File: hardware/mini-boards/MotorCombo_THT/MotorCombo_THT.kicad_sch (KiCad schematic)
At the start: 26 parts, among them J7 Conn_01x02

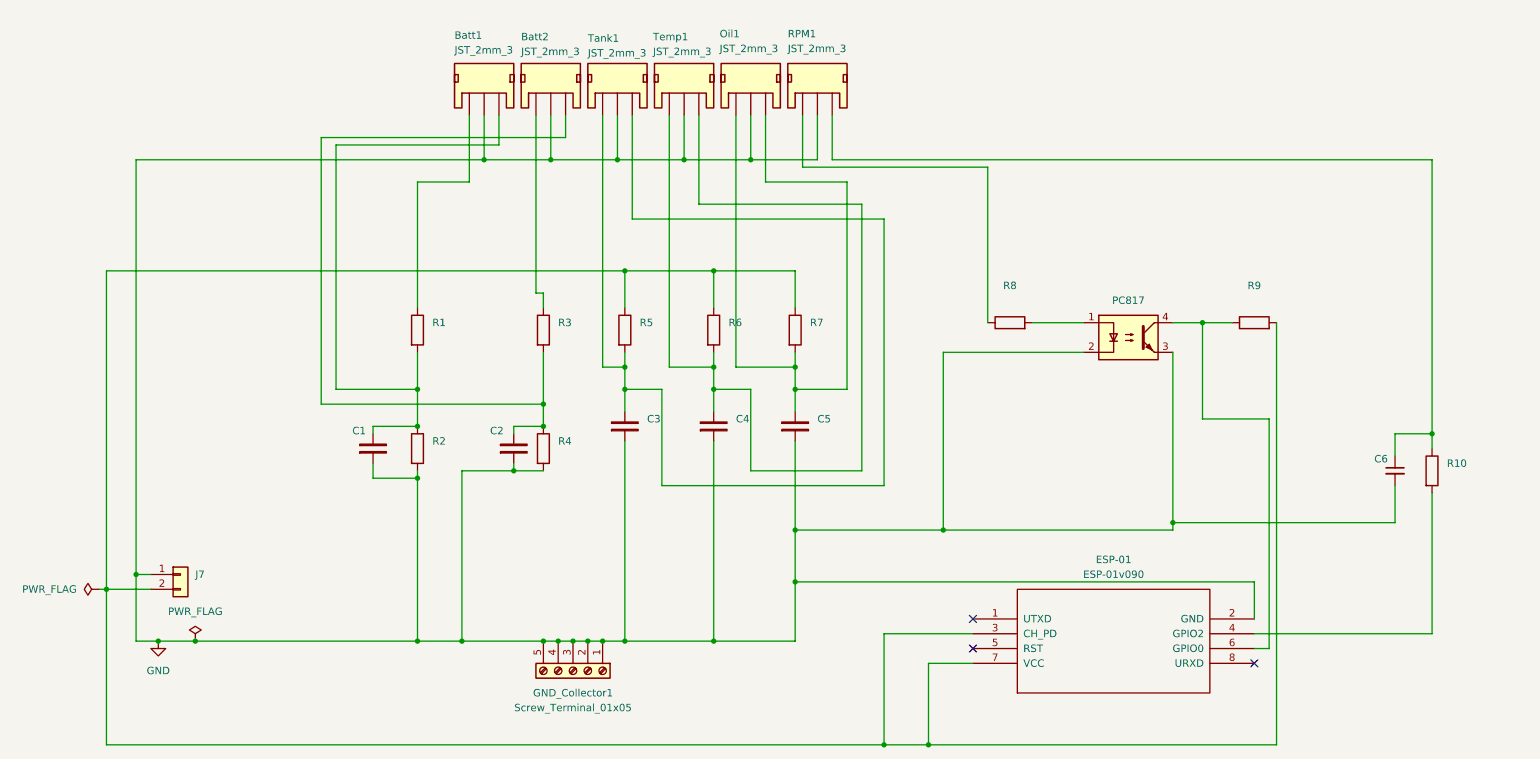
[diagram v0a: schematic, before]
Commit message: MotorCombo THT: Jumper-Doku, Rev.1-Bild, ESP-01-Firmware; SMD-Variante entfernt
- README (DE/EN): neuer Abschnitt "Kanalmodus — Jumper (Kanäle 1–5)":
  JP1 (P1=3.3V/Pullup, P3=SIG-IN/Teiler, P2=gemeinsam), JP2 und R2 wählen
  Pull-up- vs. Spannungsteiler-Modus je Kanal. Hinweis unter der Kanaltabelle.
- Neues Platinenbild MotorCombo_THT.jpg (Rev.1-Render) eingebunden.
- esp_firmware/esp_firmware.ino wiederhergestellt (ESP-01 Drehzahl: GPIO0
  Impulszählung vom Optokoppler, GPIO2 PWM zum MUX).
- KiCad-Projekt aktualisiert; alte Gerber entfernt.
- MotorCombo/ (SMD-Variante) entfernt.

Co-Authored-By: Claude Opus 4.8 <noreply@anthropic.com>
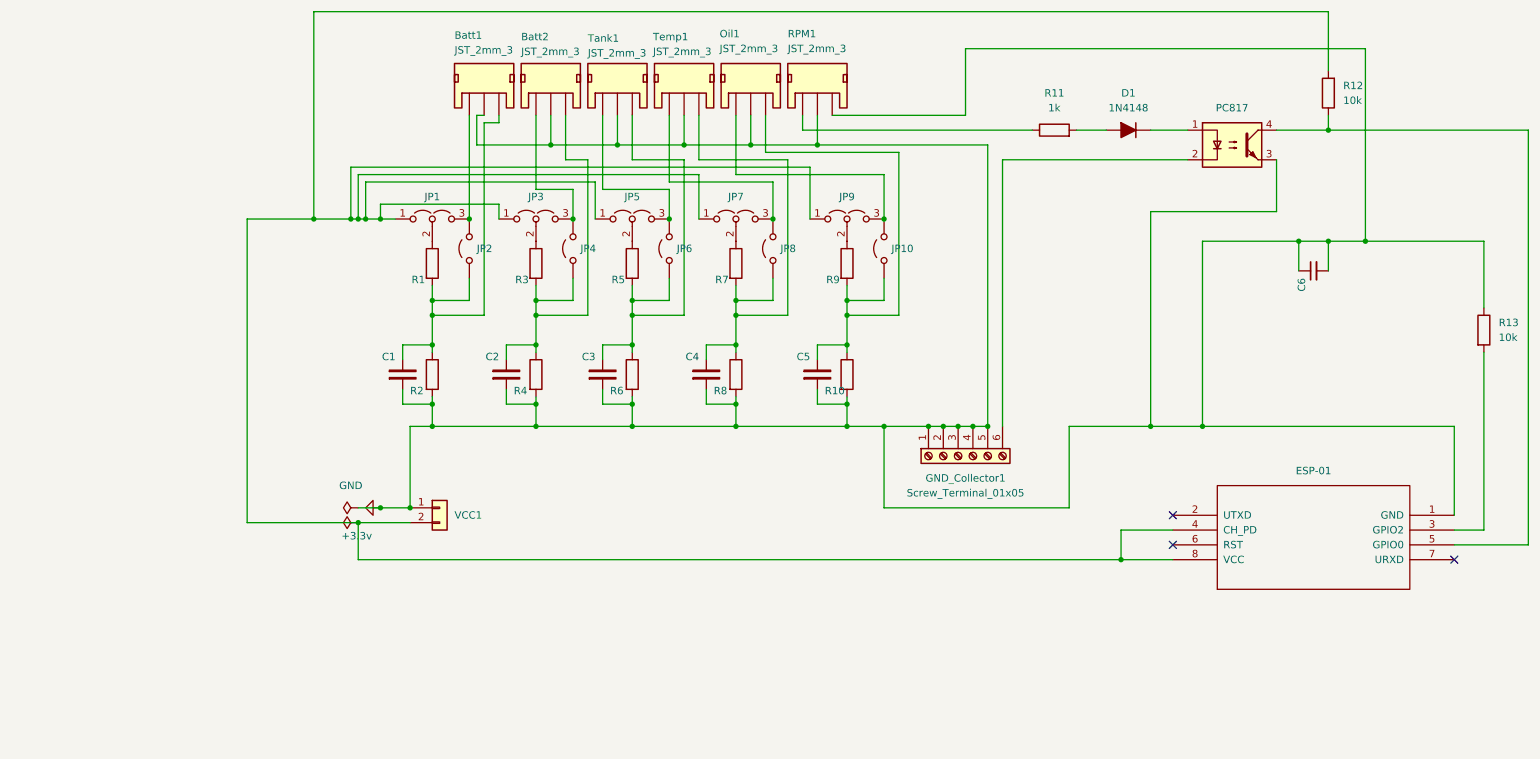
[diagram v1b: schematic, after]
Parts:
- added D1: 1N4148, PCM_Diode_THT_AKL:D_DO-35_SOD27_P7.62mm_Horizontal, symbol PCM_Diode_AKL:1N4148
- added JP1, JP3, JP5, JP7, JP9: Jumper_3_Open, PCM_SparkFun-Jumper:Jumper_3_NO_NoSilk, symbol Jumper:Jumper_3_Open
- added JP10, JP2, JP4, JP6, JP8: Jumper_2_Open, PCM_SparkFun-Jumper:Jumper_2_NO, symbol Jumper:Jumper_2_Open
- added R10, R8, R9: R, Resistor_THT:R_Axial_DIN0204_L3.6mm_D1.6mm_P7.62mm_Horizontal, symbol Device:R
- GND_Collector1: footprint TerminalBlock_Phoenix:TerminalBlock_Phoenix_MKDS-3-5-5.08_1x05_P5.08mm_Horizontal -> TerminalBlock_Phoenix:TerminalBlock_Phoenix_MKDS-3-6-5.08_1x06_P5.08mm_Horizontal; symbol Connector:Screw_Terminal_01x05 -> Connector:Screw_Terminal_01x06
- R11: renamed from R8; value R -> 1k
- R12: renamed from R9; value R -> 10k
- R13: renamed from R10; value R -> 10k
- R6: LCSC C17414 -> C17516
- renumbered J7 to VCC1
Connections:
- net GND: now also C6.1, ESP-01.1 (GND), R13.1, R6.2, RPM1.3, R10.2, R8.2; no longer ESP-01.2 (GND), PC817.2
- net at Batt1.3, C1.2, R1.2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: now also JP2.1 (A)
- net at Batt1.1: now also JP1.3 (B), JP2.2 (B); no longer R1.1
- net at R11.2: now also D1.2 (A); no longer PC817.1
- net at Batt2.3, C2.2, R3.2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: now also JP4.1 (A)
- net at C4.2, Temp1.3: now also R7.2, JP8.1 (A), R8.1; no longer R6.2, Temp1.1
- net at C5.2, Oil1.3: now also JP10.1 (A), R10.1, R9.2; no longer Oil1.1, R7.2
- net at R3.1: now also JP3.2 (C); no longer Batt2.1
- net at PC817.4, R12.1: now also ESP-01.5 (GPIO0); no longer ESP-01.6 (GPIO0)
- net at C3.2, R5.2, Tank1.3: now also R6.1, JP6.1 (A); no longer Tank1.1
- net at ESP-01.4 (CH_PD): now also ESP-01.8 (VCC), R12.2, VCC1.2 (Pin_2), JP1.1 (A), JP3.1 (A), JP5.1 (A), JP7.1 (A), JP9.1 (A); no longer R13.2
- new net: JP10.2 (B), JP9.3 (B), Oil1.1
- new net: JP7.2 (C), R7.1
- new net: JP5.2 (C), R5.1
- new net: JP7.3 (B), JP8.2 (B), Temp1.1
- new net: Batt2.1, JP3.3 (B), JP4.2 (B)
- new net: D1.1 (K), PC817.1
- new net: GND_Collector1.6 (Pin_6), PC817.2
- new net: JP5.3 (B), JP6.2 (B), Tank1.1
- new net: ESP-01.3 (GPIO2), R13.2
- new net: JP1.2 (C), R1.1
- new net: JP9.2 (C), R9.1
- now unconnected: ESP-01.7 (VCC)
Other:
- moved on the sheet: C1, C6, ESP-01, PC817, R1, R11, R12, R13, R2, VCC1
